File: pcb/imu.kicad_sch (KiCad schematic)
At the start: 4 parts, among them U26 ICM-42688-P

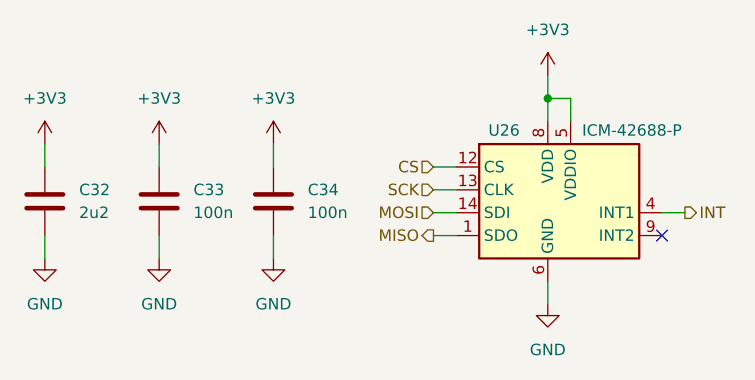
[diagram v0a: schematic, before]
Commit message: Remove sensor hub
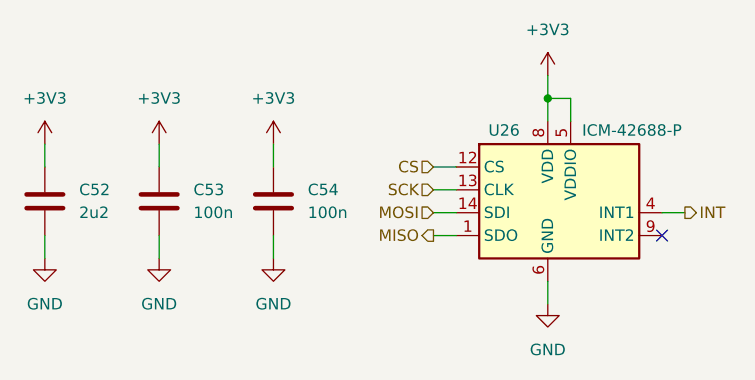
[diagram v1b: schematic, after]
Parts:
- renumbered C32 to C52, C33 to C53, C34 to C54
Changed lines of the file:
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@@
 		(dnp no)
 		(fields_autoplaced yes)
-		(property "Reference" "#PWR0162"
+		(property "Reference" "#PWR0194"
 			(at 78.74 74.93 0)
 			(effects
@@
 		(instances
 			(project "raven"
-				(path "/38b0a34b-2047-47f6-90d7-ccdf77e8e212/69f17c52-085e-4098-9317-47d7511472bd/57782601-a380-4e83-8dfa-53e09bbece77"
-					(reference "#PWR0162")
+				(path "/38b0a34b-2047-47f6-90d7-ccdf77e8e212/8ef7f6c1-b5f0-4b4e-b05a-a624501256e5"
+					(reference "#PWR071")
 					(unit 1)
 				)
@@
 		(dnp no)
 		(fields_autoplaced yes)
-		(property "Reference" "#PWR0164"
+		(property "Reference" "#PWR0196"
 			(at 109.22 80.01 0)
 			(effects
@@
 		(instances
 			(project "raven"
-				(path "/38b0a34b-2047-47f6-90d7-ccdf77e8e212/69f17c52-085e-4098-9317-47d7511472bd/57782601-a380-4e83-8dfa-53e09bbece77"
-					(reference "#PWR0164")
+				(path "/38b0a34b-2047-47f6-90d7-ccdf77e8e212/8ef7f6c1-b5f0-4b4e-b05a-a624501256e5"
+					(reference "#PWR073")
 					(unit 1)
 				)
@@
 		(dnp no)
 		(fields_autoplaced yes)
-		(property "Reference" "#PWR0161"
+		(property "Reference" "#PWR0193"
 			(at 78.74 59.69 0)
 			(effects
@@
 		(instances
 			(project "raven"
-				(path "/38b0a34b-2047-47f6-90d7-ccdf77e8e212/69f17c52-085e-4098-9317-47d7511472bd/57782601-a380-4e83-8dfa-53e09bbece77"
-					(reference "#PWR0161")
+				(path "/38b0a34b-2047-47f6-90d7-ccdf77e8e212/8ef7f6c1-b5f0-4b4e-b05a-a624501256e5"
+					(reference "#PWR070")
 					(unit 1)
 				)
@@
 		(dnp no)
 		(fields_autoplaced yes)
-		(property "Reference" "#PWR0158"
+		(property "Reference" "#PWR0190"
 			(at 53.34 74.93 0)
 			(effects
@@
 		(instances
 			(project "raven"
-				(path "/38b0a34b-2047-47f6-90d7-ccdf77e8e212/69f17c52-085e-4098-9317-47d7511472bd/57782601-a380-4e83-8dfa-53e09bbece77"
-					(reference "#PWR0158")
+				(path "/38b0a34b-2047-47f6-90d7-ccdf77e8e212/8ef7f6c1-b5f0-4b4e-b05a-a624501256e5"
+					(reference "#PWR067")
 					(unit 1)
 				)
@@
 		(dnp no)
 		(fields_autoplaced yes)
-		(property "Reference" "#PWR0157"
+		(property "Reference" "#PWR0189"
 			(at 53.34 59.69 0)
 			(effects
@@
 		(instances
 			(project "raven"
-				(path "/38b0a34b-2047-47f6-90d7-ccdf77e8e212/69f17c52-085e-4098-9317-47d7511472bd/57782601-a380-4e83-8dfa-53e09bbece77"
-					(reference "#PWR0157")
+				(path "/38b0a34b-2047-47f6-90d7-ccdf77e8e212/8ef7f6c1-b5f0-4b4e-b05a-a624501256e5"
+					(reference "#PWR066")
 					(unit 1)
 				)
@@
 		(dnp no)
 		(fields_autoplaced yes)
-		(property "Reference" "#PWR0163"
+		(property "Reference" "#PWR0195"
 			(at 109.22 52.07 0)
 			(effects
@@
 		(instances
 			(project "raven"
-				(path "/38b0a34b-2047-47f6-90d7-ccdf77e8e212/69f17c52-085e-4098-9317-47d7511472bd/57782601-a380-4e83-8dfa-53e09bbece77"
-					(reference "#PWR0163")
+				(path "/38b0a34b-2047-47f6-90d7-ccdf77e8e212/8ef7f6c1-b5f0-4b4e-b05a-a624501256e5"
+					(reference "#PWR072")
 					(unit 1)
 				)
@@
 		(dnp no)
 		(fields_autoplaced yes)
-		(property "Reference" "C33"
+		(property "Reference" "C53"
 			(at 69.85 60.9599 0)
 			(effects
@@
 		(instances
 			(project "raven"
-				(path "/38b0a34b-2047-47f6-90d7-ccdf77e8e212/69f17c52-085e-4098-9317-47d7511472bd/57782601-a380-4e83-8dfa-53e09bbece77"
-					(reference "C33")
+				(path "/38b0a34b-2047-47f6-90d7-ccdf77e8e212/8ef7f6c1-b5f0-4b4e-b05a-a624501256e5"
+					(reference "C19")
 					(unit 1)
 				)
@@
 		(dnp no)
 		(fields_autoplaced yes)
-		(property "Reference" "#PWR0159"
+		(property "Reference" "#PWR0191"
 			(at 66.04 59.69 0)
 			(effects
@@
 		(instances
 			(project "raven"
-				(path "/38b0a34b-2047-47f6-90d7-ccdf77e8e212/69f17c52-085e-4098-9317-47d7511472bd/57782601-a380-4e83-8dfa-53e09bbece77"
-					(reference "#PWR0159")
+				(path "/38b0a34b-2047-47f6-90d7-ccdf77e8e212/8ef7f6c1-b5f0-4b4e-b05a-a624501256e5"
+					(reference "#PWR068")
 					(unit 1)
 				)
@@
 		(dnp no)
 		(fields_autoplaced yes)
-		(property "Reference" "C34"
+		(property "Reference" "C54"
 			(at 82.55 60.9599 0)
 			(effects
@@
 		(instances
 			(project "raven"
-				(path "/38b0a34b-2047-47f6-90d7-ccdf77e8e212/69f17c52-085e-4098-9317-47d7511472bd/57782601-a380-4e83-8dfa-53e09bbece77"
-					(reference "C34")
+				(path "/38b0a34b-2047-47f6-90d7-ccdf77e8e212/8ef7f6c1-b5f0-4b4e-b05a-a624501256e5"
+					(reference "C20")
 					(unit 1)
 				)
@@
 		(dnp no)
 		(fields_autoplaced yes)
-		(property "Reference" "C32"
+		(property "Reference" "C52"
 			(at 57.15 60.9599 0)
 			(effects
@@
 		(instances
 			(project "raven"
-				(path "/38b0a34b-2047-47f6-90d7-ccdf77e8e212/69f17c52-085e-4098-9317-47d7511472bd/57782601-a380-4e83-8dfa-53e09bbece77"
-					(reference "C32")
+				(path "/38b0a34b-2047-47f6-90d7-ccdf77e8e212/8ef7f6c1-b5f0-4b4e-b05a-a624501256e5"
+					(reference "C18")
 					(unit 1)
 				)
@@
 		(dnp no)
 		(fields_autoplaced yes)
-		(property "Reference" "#PWR0160"
+		(property "Reference" "#PWR0192"
 			(at 66.04 74.93 0)
 			(effects
@@
 		(instances
 			(project "raven"
-				(path "/38b0a34b-2047-47f6-90d7-ccdf77e8e212/69f17c52-085e-4098-9317-47d7511472bd/57782601-a380-4e83-8dfa-53e09bbece77"
-					(reference "#PWR0160")
+				(path "/38b0a34b-2047-47f6-90d7-ccdf77e8e212/8ef7f6c1-b5f0-4b4e-b05a-a624501256e5"
+					(reference "#PWR069")
 					(unit 1)
 				)
@@
 		(instances
 			(project "raven"
-				(path "/38b0a34b-2047-47f6-90d7-ccdf77e8e212/69f17c52-085e-4098-9317-47d7511472bd/57782601-a380-4e83-8dfa-53e09bbece77"
-					(reference "U26")
-					(unit 1)
-				)
+				(path "/38b0a34b-2047-47f6-90d7-ccdf77e8e212/8ef7f6c1-b5f0-4b4e-b05a-a624501256e5"
+					(reference "U8")
+					(unit 1)
+				)

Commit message: Finish schematic
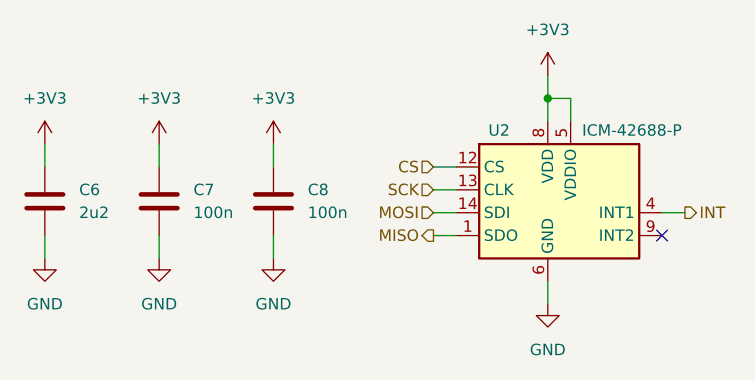
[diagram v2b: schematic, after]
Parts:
- renumbered C52 to C6, C53 to C7, C54 to C8, U26 to U2
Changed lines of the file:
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@@
 		(dnp no)
 		(fields_autoplaced yes)
-		(property "Reference" "#PWR0194"
+		(property "Reference" "#PWR034"
 			(at 78.74 74.93 0)
 			(effects
@@
 			(project "raven"
 				(path "/38b0a34b-2047-47f6-90d7-ccdf77e8e212/8ef7f6c1-b5f0-4b4e-b05a-a624501256e5"
-					(reference "#PWR071")
+					(reference "#PWR034")
 					(unit 1)
 				)
@@
 		(dnp no)
 		(fields_autoplaced yes)
-		(property "Reference" "#PWR0196"
+		(property "Reference" "#PWR036"
 			(at 109.22 80.01 0)
 			(effects
@@
 			(project "raven"
 				(path "/38b0a34b-2047-47f6-90d7-ccdf77e8e212/8ef7f6c1-b5f0-4b4e-b05a-a624501256e5"
-					(reference "#PWR073")
+					(reference "#PWR036")
 					(unit 1)
 				)
@@
 		(dnp no)
 		(fields_autoplaced yes)
-		(property "Reference" "#PWR0193"
+		(property "Reference" "#PWR033"
 			(at 78.74 59.69 0)
 			(effects
@@
 			(project "raven"
 				(path "/38b0a34b-2047-47f6-90d7-ccdf77e8e212/8ef7f6c1-b5f0-4b4e-b05a-a624501256e5"
-					(reference "#PWR070")
+					(reference "#PWR033")
 					(unit 1)
 				)
@@
 		(dnp no)
 		(fields_autoplaced yes)
-		(property "Reference" "#PWR0190"
+		(property "Reference" "#PWR030"
 			(at 53.34 74.93 0)
 			(effects
@@
 			(project "raven"
 				(path "/38b0a34b-2047-47f6-90d7-ccdf77e8e212/8ef7f6c1-b5f0-4b4e-b05a-a624501256e5"
-					(reference "#PWR067")
+					(reference "#PWR030")
 					(unit 1)
 				)
@@
 		(dnp no)
 		(fields_autoplaced yes)
-		(property "Reference" "#PWR0189"
+		(property "Reference" "#PWR029"
 			(at 53.34 59.69 0)
 			(effects
@@
 			(project "raven"
 				(path "/38b0a34b-2047-47f6-90d7-ccdf77e8e212/8ef7f6c1-b5f0-4b4e-b05a-a624501256e5"
-					(reference "#PWR066")
+					(reference "#PWR029")
 					(unit 1)
 				)
@@
 		(dnp no)
 		(fields_autoplaced yes)
-		(property "Reference" "#PWR0195"
+		(property "Reference" "#PWR035"
 			(at 109.22 52.07 0)
 			(effects
@@
 			(project "raven"
 				(path "/38b0a34b-2047-47f6-90d7-ccdf77e8e212/8ef7f6c1-b5f0-4b4e-b05a-a624501256e5"
-					(reference "#PWR072")
+					(reference "#PWR035")
 					(unit 1)
 				)
@@
 		(dnp no)
 		(fields_autoplaced yes)
-		(property "Reference" "C53"
+		(property "Reference" "C7"
 			(at 69.85 60.9599 0)
 			(effects
@@
 			(project "raven"
 				(path "/38b0a34b-2047-47f6-90d7-ccdf77e8e212/8ef7f6c1-b5f0-4b4e-b05a-a624501256e5"
-					(reference "C19")
+					(reference "C7")
 					(unit 1)
 				)
@@
 		(dnp no)
 		(fields_autoplaced yes)
-		(property "Reference" "#PWR0191"
+		(property "Reference" "#PWR031"
 			(at 66.04 59.69 0)
 			(effects
@@
 			(project "raven"
 				(path "/38b0a34b-2047-47f6-90d7-ccdf77e8e212/8ef7f6c1-b5f0-4b4e-b05a-a624501256e5"
-					(reference "#PWR068")
+					(reference "#PWR031")
 					(unit 1)
 				)
@@
 		(dnp no)
 		(fields_autoplaced yes)
-		(property "Reference" "C54"
+		(property "Reference" "C8"
 			(at 82.55 60.9599 0)
 			(effects
@@
 			(project "raven"
 				(path "/38b0a34b-2047-47f6-90d7-ccdf77e8e212/8ef7f6c1-b5f0-4b4e-b05a-a624501256e5"
-					(reference "C20")
+					(reference "C8")
 					(unit 1)
 				)
@@
 		(dnp no)
 		(fields_autoplaced yes)
-		(property "Reference" "C52"
+		(property "Reference" "C6"
 			(at 57.15 60.9599 0)
 			(effects
@@
 			(project "raven"
 				(path "/38b0a34b-2047-47f6-90d7-ccdf77e8e212/8ef7f6c1-b5f0-4b4e-b05a-a624501256e5"
-					(reference "C18")
+					(reference "C6")
 					(unit 1)
 				)
@@
 		(dnp no)
 		(fields_autoplaced yes)
-		(property "Reference" "#PWR0192"
+		(property "Reference" "#PWR032"
 			(at 66.04 74.93 0)
 			(effects
@@
 			(project "raven"
 				(path "/38b0a34b-2047-47f6-90d7-ccdf77e8e212/8ef7f6c1-b5f0-4b4e-b05a-a624501256e5"
-					(reference "#PWR069")
+					(reference "#PWR032")
 					(unit 1)
 				)
@@
 		(on_board yes)
 		(dnp no)
-		(property "Reference" "U26"
+		(property "Reference" "U2"
 			(at 102.616 54.356 0)
 			(effects
@@
 			(project "raven"
 				(path "/38b0a34b-2047-47f6-90d7-ccdf77e8e212/8ef7f6c1-b5f0-4b4e-b05a-a624501256e5"
-					(reference "U8")
-					(unit 1)
-				)
+					(reference "U2")
+					(unit 1)
+				)

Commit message: Finish schematic
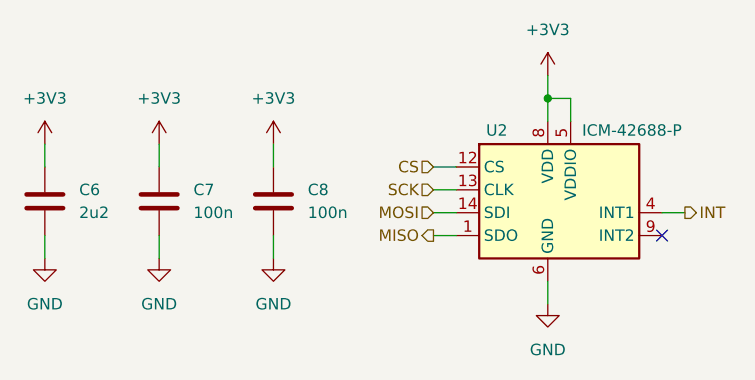
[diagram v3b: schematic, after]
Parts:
- removed U2: ICM-42688-P, Package_LGA:LGA-14_3x2.5mm_P0.5mm_LayoutBorder3x4y, symbol User_Symbols:ICM-42688-P
- added U2: ICM-42688-P, Package_LGA:LGA-14_3x2.5mm_P0.5mm_LayoutBorder3x4y, symbol Symbols:ICM-42688-P
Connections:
- net +3V3: now also U2.5 (VDDIO), U2.8 (VDD)
- net CS: now also U2.12 (CS)
- net GND: now also U2.11 (RESV), U2.6 (GND), U2.7 (RESV)
- net INT: now also U2.4 (INT1)
- net MISO: now also U2.1 (SDO)
- net MOSI: now also U2.14 (SDI)
- net SCK: now also U2.13 (CLK)
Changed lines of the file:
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@@
+	)
+	(symbol
+		(lib_id "Symbols:ICM-42688-P")
+		(at 101.6 55.88 0)
+		(unit 1)
+		(exclude_from_sim no)
+		(in_bom yes)
+		(on_board yes)
+		(dnp no)
+		(property "Reference" "U2"
+			(at 102.362 54.356 0)
+			(effects
+				(font
+					(size 1.27 1.27)
+				)
+				(justify left)
+			)
+		)
+		(property "Value" "ICM-42688-P"
+			(at 113.03 54.356 0)
+			(effects
+				(font
+					(size 1.27 1.27)
+				)
+				(justify left)
+			)
+		)
+		(property "Footprint" "Package_LGA:LGA-14_3x2.5mm_P0.5mm_LayoutBorder3x4y"
+			(at 110.744 42.418 0)
+			(effects
+				(font
+					(size 1.27 1.27)
+				)
+				(hide yes)
+			)
+		)
+		(property "Datasheet" "https://wmsc.lcsc.com/wmsc/upload/file/pdf/v2/lcsc/2108030230_TDK-InvenSense-ICM-42688-P_C1850418.pdf"
+			(at 110.744 39.878 0)
+			(effects
+				(font
+					(size 1.27 1.27)
+				)
+				(hide yes)
+			)
+		)
+		(property "Description" "IMU Gyroscope"
+			(at 110.744 37.338 0)
+			(effects
+				(font
+					(size 1.27 1.27)
+				)
+				(hide yes)
+			)
+		)
+		(pin "9"
+		)
+		(pin "12"
+		)
+		(pin "11"
+		)
+		(pin "3"
+		)
+		(pin "5"
+		)
+		(pin "13"
+		)
+		(pin "14"
+		)
+		(pin "2"
+		)
+		(pin "4"
+		)
+		(pin "1"
+		)
+		(pin "7"
+		)
+		(pin "6"
+		)
+		(pin "8"
+		)
+		(pin "10"
+		)
+		(instances
+			(project ""
+				(path "/38b0a34b-2047-47f6-90d7-ccdf77e8e212/8ef7f6c1-b5f0-4b4e-b05a-a624501256e5"
+					(reference "U2")
+					(unit 1)
+				)
+			)
+		)
 	)
 	(symbol
@@
 					(unit 1)
 				)
-			)
-		)
-	)
-	(symbol
-		(lib_id "User_Symbols:ICM-42688-P")
-		(at 101.6 55.88 0)
-		(unit 1)
-		(exclude_from_sim no)
-		(in_bom yes)
-		(on_board yes)
-		(dnp no)
-		(property "Reference" "U2"
-			(at 102.616 54.356 0)
-			(effects
-				(font
-					(size 1.27 1.27)
-				)
-				(justify left)
-			)
-		)
-		(property "Value" "ICM-42688-P"
-			(at 113.03 54.356 0)
-			(effects
-				(font
-					(size 1.27 1.27)
-				)
-				(justify left)
-			)
-		)
-		(property "Footprint" "Package_LGA:LGA-14_3x2.5mm_P0.5mm_LayoutBorder3x4y"
-			(at 104.14 45.72 0)
-			(effects
-				(font
-					(size 1.27 1.27)
-				)
-				(hide yes)
-			)
-		)
-		(property "Datasheet" "https://wmsc.lcsc.com/wmsc/upload/file/pdf/v2/lcsc/2108030230_TDK-InvenSense-ICM-42688-P_C1850418.pdf"
-			(at 107.95 43.18 0)
-			(effects
-				(font
-					(size 1.27 1.27)
-				)
-				(hide yes)
-			)
-		)
-		(property "Description" "IMU Gyroscope"
-			(at 101.6 40.64 0)
-			(effects
-				(font
-					(size 1.27 1.27)
-				)
-				(hide yes)
-			)
-		)
-		(property "LCSC" "C1850418"
-			(at 101.6 55.88 0)
-			(effects
-				(font
-					(size 1.27 1.27)
-				)
-				(hide yes)
-			)
-		)
-		(pin "3"
-		)
-		(pin "9"
-		)
-		(pin "7"
-		)
-		(pin "5"
-		)
-		(pin "8"
-		)
-		(pin "11"
-		)
-		(pin "1"
-		)
-		(pin "6"
-		)
-		(pin "12"
-		)
-		(pin "2"
-		)
-		(pin "10"
-		)
-		(pin "4"
-		)
-		(pin "13"
-		)
-		(pin "14"
-		)
-		(instances
-			(project "raven"
-				(path "/38b0a34b-2047-47f6-90d7-ccdf77e8e212/8ef7f6c1-b5f0-4b4e-b05a-a624501256e5"
-					(reference "U2")
-					(unit 1)
-				)

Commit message: Plan adding power switch
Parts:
- U2: LCSC (none) -> C1850418
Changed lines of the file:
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@@
+			)
+		)
+		(property "LCSC" "C1850418"
+			(at 101.6 55.88 0)
+			(effects
+				(font
+					(size 1.27 1.27)
+				)
+				(hide yes)
 			)
 		)
